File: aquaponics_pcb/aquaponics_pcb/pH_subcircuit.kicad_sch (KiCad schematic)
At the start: 4 parts, among them J1 RFPC-SMA27-F, U1 Atlas Scientific EZO

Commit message: finish MCU and start logic isolation block
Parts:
- J1: footprint RFPCSMA27F -> SamacSys_Parts:RFPCSMA27F
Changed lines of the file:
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@@
 			)
 		)
-		(property "Footprint" "RFPCSMA27F"
+		(property "Footprint" "SamacSys_Parts:RFPCSMA27F"
 			(at 179.07 187.63 0)
 			(effects

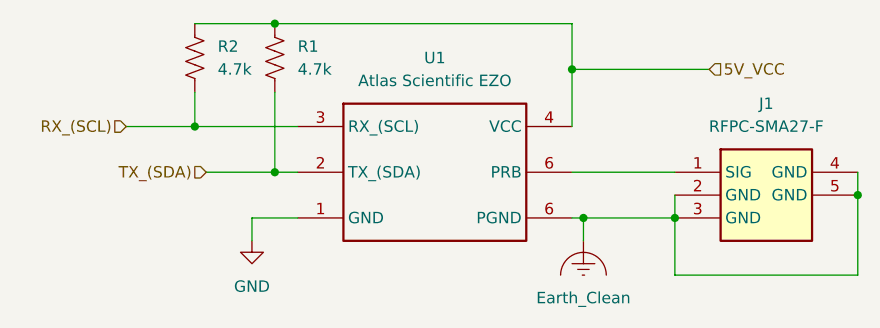
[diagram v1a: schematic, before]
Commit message: begin motor control sch
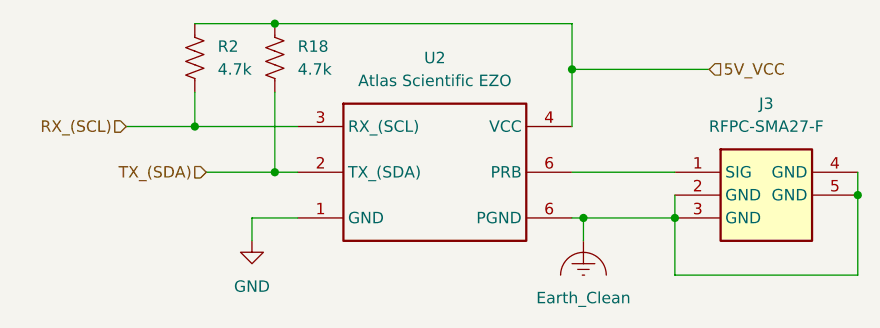
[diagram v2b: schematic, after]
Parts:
- renumbered J1 to J3, R1 to R18, U1 to U2
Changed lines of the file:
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@@
 		(instances
 			(project "aquaponics_pcb"
+				(path "/c5e5a8d2-0dcc-4520-98a5-511e1dc0d12f/07c81ada-4777-4a98-b82e-c983cee6a37c"
+					(reference "R17")
+					(unit 1)
+				)
 				(path "/c5e5a8d2-0dcc-4520-98a5-511e1dc0d12f/37a12f26-e0b7-4740-be24-dc513a8a30de"
 					(reference "R2")
+					(unit 1)
+				)
+				(path "/c5e5a8d2-0dcc-4520-98a5-511e1dc0d12f/a6edc2ac-dd2e-4ead-b353-200a5e98d0aa"
+					(reference "R1")
 					(unit 1)
 				)
@@
 		(dnp no)
 		(fields_autoplaced yes)
-		(property "Reference" "#PWR02"
+		(property "Reference" "#PWR027"
 			(at 152.4 107.95 0)
 			(effects
@@
 		)
 		(instances
-			(project ""
-				(path "/c5e5a8d2-0dcc-4520-98a5-511e1dc0d12f/37a12f26-e0b7-4740-be24-dc513a8a30de"
+			(project "aquaponics_pcb"
+				(path "/c5e5a8d2-0dcc-4520-98a5-511e1dc0d12f/07c81ada-4777-4a98-b82e-c983cee6a37c"
+					(reference "#PWR027")
+					(unit 1)
+				)
+				(path "/c5e5a8d2-0dcc-4520-98a5-511e1dc0d12f/37a12f26-e0b7-4740-be24-dc513a8a30de"
+					(reference "#PWR027")
+					(unit 1)
+				)
+				(path "/c5e5a8d2-0dcc-4520-98a5-511e1dc0d12f/a6edc2ac-dd2e-4ead-b353-200a5e98d0aa"
 					(reference "#PWR02")
 					(unit 1)
@@
 		(dnp no)
 		(fields_autoplaced yes)
-		(property "Reference" "U1"
+		(property "Reference" "U2"
 			(at 135.89 80.01 0)
 			(effects
@@
 		)
 		(instances
-			(project ""
-				(path "/c5e5a8d2-0dcc-4520-98a5-511e1dc0d12f/37a12f26-e0b7-4740-be24-dc513a8a30de"
+			(project "aquaponics_pcb"
+				(path "/c5e5a8d2-0dcc-4520-98a5-511e1dc0d12f/07c81ada-4777-4a98-b82e-c983cee6a37c"
+					(reference "U2")
+					(unit 1)
+				)
+				(path "/c5e5a8d2-0dcc-4520-98a5-511e1dc0d12f/37a12f26-e0b7-4740-be24-dc513a8a30de"
+					(reference "U2")
+					(unit 1)
+				)
+				(path "/c5e5a8d2-0dcc-4520-98a5-511e1dc0d12f/a6edc2ac-dd2e-4ead-b353-200a5e98d0aa"
 					(reference "U1")
 					(unit 1)
@@
 		(dnp no)
 		(fields_autoplaced yes)
-		(property "Reference" "R1"
+		(property "Reference" "R18"
 			(at 120.65 78.7399 0)
 			(effects
@@
 		)
 		(instances
-			(project ""
-				(path "/c5e5a8d2-0dcc-4520-98a5-511e1dc0d12f/37a12f26-e0b7-4740-be24-dc513a8a30de"
-					(reference "R1")
+			(project "aquaponics_pcb"
+				(path "/c5e5a8d2-0dcc-4520-98a5-511e1dc0d12f/07c81ada-4777-4a98-b82e-c983cee6a37c"
+					(reference "R18")
+					(unit 1)
+				)
+				(path "/c5e5a8d2-0dcc-4520-98a5-511e1dc0d12f/37a12f26-e0b7-4740-be24-dc513a8a30de"
+					(reference "R18")
+					(unit 1)
+				)
+				(path "/c5e5a8d2-0dcc-4520-98a5-511e1dc0d12f/a6edc2ac-dd2e-4ead-b353-200a5e98d0aa"
+					(reference "R19")
 					(unit 1)
 				)
@@
 		(dnp no)
 		(fields_autoplaced yes)
-		(property "Reference" "J1"
+		(property "Reference" "J3"
 			(at 172.72 85.09 0)
 			(effects
@@
 		)
 		(instances
-			(project ""
-				(path "/c5e5a8d2-0dcc-4520-98a5-511e1dc0d12f/37a12f26-e0b7-4740-be24-dc513a8a30de"
+			(project "aquaponics_pcb"
+				(path "/c5e5a8d2-0dcc-4520-98a5-511e1dc0d12f/07c81ada-4777-4a98-b82e-c983cee6a37c"
+					(reference "J3")
+					(unit 1)
+				)
+				(path "/c5e5a8d2-0dcc-4520-98a5-511e1dc0d12f/37a12f26-e0b7-4740-be24-dc513a8a30de"
+					(reference "J3")
+					(unit 1)
+				)
+				(path "/c5e5a8d2-0dcc-4520-98a5-511e1dc0d12f/a6edc2ac-dd2e-4ead-b353-200a5e98d0aa"
 					(reference "J1")
 					(unit 1)
@@
 		(dnp no)
 		(fields_autoplaced yes)
-		(property "Reference" "#PWR01"
+		(property "Reference" "#PWR026"
 			(at 115.57 106.68 0)
 			(effects
@@
 		)
 		(instances
-			(project ""
-				(path "/c5e5a8d2-0dcc-4520-98a5-511e1dc0d12f/37a12f26-e0b7-4740-be24-dc513a8a30de"
+			(project "aquaponics_pcb"
+				(path "/c5e5a8d2-0dcc-4520-98a5-511e1dc0d12f/07c81ada-4777-4a98-b82e-c983cee6a37c"
+					(reference "#PWR026")
+					(unit 1)
+				)
+				(path "/c5e5a8d2-0dcc-4520-98a5-511e1dc0d12f/37a12f26-e0b7-4740-be24-dc513a8a30de"
+					(reference "#PWR026")
+					(unit 1)
+				)
+				(path "/c5e5a8d2-0dcc-4520-98a5-511e1dc0d12f/a6edc2ac-dd2e-4ead-b353-200a5e98d0aa"
 					(reference "#PWR01")
 					(unit 1)

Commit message: add ezo datasheets, update motor schematic and add 2 motors
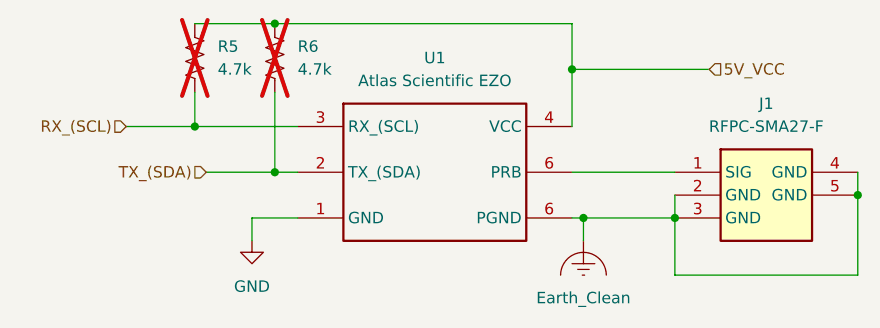
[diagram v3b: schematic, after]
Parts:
- R5: renamed from R2; now not fitted
- R6: renamed from R18; now not fitted
- renumbered J3 to J1, U2 to U1
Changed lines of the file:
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@@
 		(in_bom yes)
 		(on_board yes)
-		(dnp no)
+		(dnp yes)
 		(fields_autoplaced yes)
-		(property "Reference" "R2"
+		(property "Reference" "R5"
 			(at 111.76 78.7399 0)
 			(effects
@@
 			(project "aquaponics_pcb"
 				(path "/c5e5a8d2-0dcc-4520-98a5-511e1dc0d12f/07c81ada-4777-4a98-b82e-c983cee6a37c"
-					(reference "R17")
+					(reference "R19")
 					(unit 1)
 				)
 				(path "/c5e5a8d2-0dcc-4520-98a5-511e1dc0d12f/37a12f26-e0b7-4740-be24-dc513a8a30de"
-					(reference "R2")
+					(reference "R5")
 					(unit 1)
 				)
 				(path "/c5e5a8d2-0dcc-4520-98a5-511e1dc0d12f/a6edc2ac-dd2e-4ead-b353-200a5e98d0aa"
-					(reference "R1")
+					(reference "R21")
 					(unit 1)
 				)
@@
 		(dnp no)
 		(fields_autoplaced yes)
-		(property "Reference" "#PWR027"
+		(property "Reference" "#PWR02"
 			(at 152.4 107.95 0)
 			(effects
@@
 			(project "aquaponics_pcb"
 				(path "/c5e5a8d2-0dcc-4520-98a5-511e1dc0d12f/07c81ada-4777-4a98-b82e-c983cee6a37c"
-					(reference "#PWR027")
+					(reference "#PWR030")
 					(unit 1)
 				)
 				(path "/c5e5a8d2-0dcc-4520-98a5-511e1dc0d12f/37a12f26-e0b7-4740-be24-dc513a8a30de"
-					(reference "#PWR027")
+					(reference "#PWR02")
 					(unit 1)
 				)
 				(path "/c5e5a8d2-0dcc-4520-98a5-511e1dc0d12f/a6edc2ac-dd2e-4ead-b353-200a5e98d0aa"
-					(reference "#PWR02")
+					(reference "#PWR032")
 					(unit 1)
 				)
@@
 		(dnp no)
 		(fields_autoplaced yes)
-		(property "Reference" "U2"
+		(property "Reference" "U1"
 			(at 135.89 80.01 0)
 			(effects
@@
 				)
 				(path "/c5e5a8d2-0dcc-4520-98a5-511e1dc0d12f/37a12f26-e0b7-4740-be24-dc513a8a30de"
-					(reference "U2")
+					(reference "U1")
 					(unit 1)
 				)
 				(path "/c5e5a8d2-0dcc-4520-98a5-511e1dc0d12f/a6edc2ac-dd2e-4ead-b353-200a5e98d0aa"
-					(reference "U1")
+					(reference "U3")
 					(unit 1)
 				)
@@
 		(in_bom yes)
 		(on_board yes)
-		(dnp no)
+		(dnp yes)
 		(fields_autoplaced yes)
-		(property "Reference" "R18"
+		(property "Reference" "R6"
 			(at 120.65 78.7399 0)
 			(effects
@@
 			(project "aquaponics_pcb"
 				(path "/c5e5a8d2-0dcc-4520-98a5-511e1dc0d12f/07c81ada-4777-4a98-b82e-c983cee6a37c"
-					(reference "R18")
+					(reference "R20")
 					(unit 1)
 				)
 				(path "/c5e5a8d2-0dcc-4520-98a5-511e1dc0d12f/37a12f26-e0b7-4740-be24-dc513a8a30de"
-					(reference "R18")
+					(reference "R6")
 					(unit 1)
 				)
 				(path "/c5e5a8d2-0dcc-4520-98a5-511e1dc0d12f/a6edc2ac-dd2e-4ead-b353-200a5e98d0aa"
-					(reference "R19")
+					(reference "R22")
 					(unit 1)
 				)
@@
 		(dnp no)
 		(fields_autoplaced yes)
-		(property "Reference" "J3"
+		(property "Reference" "J1"
 			(at 172.72 85.09 0)
 			(effects
@@
 				)
 				(path "/c5e5a8d2-0dcc-4520-98a5-511e1dc0d12f/37a12f26-e0b7-4740-be24-dc513a8a30de"
-					(reference "J3")
+					(reference "J1")
 					(unit 1)
 				)
 				(path "/c5e5a8d2-0dcc-4520-98a5-511e1dc0d12f/a6edc2ac-dd2e-4ead-b353-200a5e98d0aa"
-					(reference "J1")
+					(reference "J4")
 					(unit 1)
 				)
@@
 		(dnp no)
 		(fields_autoplaced yes)
-		(property "Reference" "#PWR026"
+		(property "Reference" "#PWR01"
 			(at 115.57 106.68 0)
 			(effects
@@
 			(project "aquaponics_pcb"
 				(path "/c5e5a8d2-0dcc-4520-98a5-511e1dc0d12f/07c81ada-4777-4a98-b82e-c983cee6a37c"
-					(reference "#PWR026")
+					(reference "#PWR029")
 					(unit 1)
 				)
 				(path "/c5e5a8d2-0dcc-4520-98a5-511e1dc0d12f/37a12f26-e0b7-4740-be24-dc513a8a30de"
-					(reference "#PWR026")
+					(reference "#PWR01")
 					(unit 1)
 				)
 				(path "/c5e5a8d2-0dcc-4520-98a5-511e1dc0d12f/a6edc2ac-dd2e-4ead-b353-200a5e98d0aa"
-					(reference "#PWR01")
-					(unit 1)
-				)
+					(reference "#PWR031")
+					(unit 1)
+				)

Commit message: add initial pcb layout
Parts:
- U1: footprint (none) -> aquaponics_pcb:EZO FOOTPRINT
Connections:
- net at J1.1 (SIG): now also U1.5 (PRB); no longer U1.6 (PRB)
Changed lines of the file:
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@@
 			)
 		)
-		(property "Footprint" ""
+		(property "Footprint" "aquaponics_pcb:EZO FOOTPRINT"
 			(at 125.73 100.33 0)
 			(effects
@@
 		(pin "4"
 		)
-		(pin "6"
+		(pin "5"
 		)
 		(instances

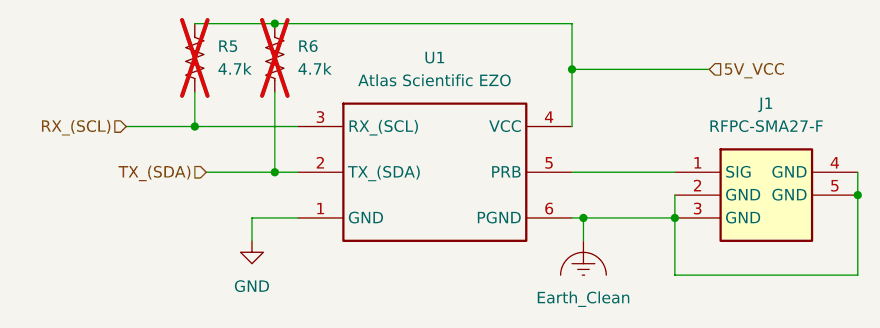
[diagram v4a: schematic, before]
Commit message: Update PCB: add ADM3260, replace C3 with SMA connector
Replaced C3 capacitor footprint with an RFPC-SMA27-F SMA connector and added the ADM3260ARSZ digital isolator (IC3) to the PCB. Updated R3 to a 10k resistor and made related netlist and footprint changes.
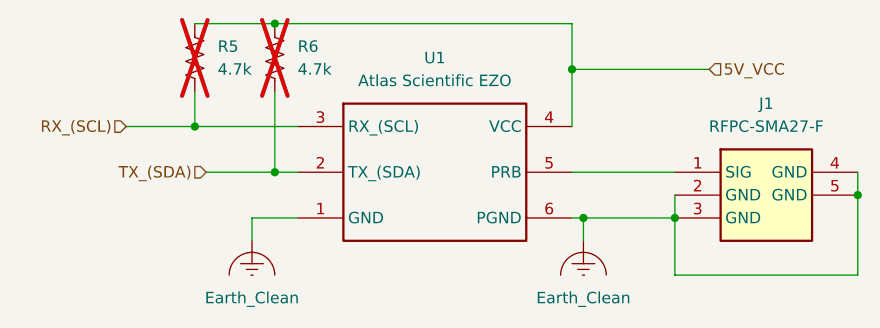
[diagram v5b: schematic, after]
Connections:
- net GND is gone; now on net Earth_Clean: U1.1 (GND)
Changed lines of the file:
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@@
+	(symbol
+		(lib_id "power:Earth_Clean")
+		(at 115.57 100.33 0)
+		(unit 1)
+		(exclude_from_sim no)
+		(in_bom yes)
+		(on_board yes)
+		(dnp no)
+		(fields_autoplaced yes)
+		(property "Reference" "#PWR01"
+			(at 115.57 107.95 0)
+			(effects
+				(font
+					(size 1.27 1.27)
+				)
+				(hide yes)
+			)
+		)
+		(property "Value" "Earth_Clean"
+			(at 115.57 106.68 0)
+			(effects
+				(font
+					(size 1.27 1.27)
+				)
+			)
+		)
+		(property "Footprint" ""
+			(at 115.57 101.6 0)
+			(effects
+				(font
+					(size 1.27 1.27)
+				)
+				(hide yes)
+			)
+		)
+		(property "Datasheet" "~"
+			(at 115.57 101.6 0)
+			(effects
+				(font
+					(size 1.27 1.27)
+				)
+				(hide yes)
+			)
+		)
+		(property "Description" "Power symbol creates a global label with name \"Earth_Clean\""
+			(at 115.57 100.33 0)
+			(effects
+				(font
+					(size 1.27 1.27)
+				)
+				(hide yes)
+			)
+		)
+		(pin "1"
+		)
+		(instances
+			(project "aquaponics_pcb"
+				(path "/c5e5a8d2-0dcc-4520-98a5-511e1dc0d12f/07c81ada-4777-4a98-b82e-c983cee6a37c"
+					(reference "#PWR029")
+					(unit 1)
+				)
+				(path "/c5e5a8d2-0dcc-4520-98a5-511e1dc0d12f/37a12f26-e0b7-4740-be24-dc513a8a30de"
+					(reference "#PWR01")
+					(unit 1)
+				)
+				(path "/c5e5a8d2-0dcc-4520-98a5-511e1dc0d12f/a6edc2ac-dd2e-4ead-b353-200a5e98d0aa"
+					(reference "#PWR031")
+					(unit 1)
+				)
+			)
+		)
+	)
 	(symbol
 		(lib_id "power:Earth_Clean")
@@
 					(unit 1)
 				)
-			)
-		)
-	)
-	(symbol
-		(lib_id "power:GND")
-		(at 115.57 100.33 0)
-		(unit 1)
-		(exclude_from_sim no)
-		(in_bom yes)
-		(on_board yes)
-		(dnp no)
-		(fields_autoplaced yes)
-		(property "Reference" "#PWR01"
-			(at 115.57 106.68 0)
-			(effects
-				(font
-					(size 1.27 1.27)
-				)
-				(hide yes)
-			)
-		)
-		(property "Value" "GND"
-			(at 115.57 105.41 0)
-			(effects
-				(font
-					(size 1.27 1.27)
-				)
-			)
-		)
-		(property "Footprint" ""
-			(at 115.57 100.33 0)
-			(effects
-				(font
-					(size 1.27 1.27)
-				)
-				(hide yes)
-			)
-		)
-		(property "Datasheet" ""
-			(at 115.57 100.33 0)
-			(effects
-				(font
-					(size 1.27 1.27)
-				)
-				(hide yes)
-			)
-		)
-		(property "Description" "Power symbol creates a global label with name \"GND\" , ground"
-			(at 115.57 100.33 0)
-			(effects
-				(font
-					(size 1.27 1.27)
-				)
-				(hide yes)
-			)
-		)
-		(pin "1"
-		)
-		(instances
-			(project "aquaponics_pcb"
-				(path "/c5e5a8d2-0dcc-4520-98a5-511e1dc0d12f/07c81ada-4777-4a98-b82e-c983cee6a37c"
-					(reference "#PWR029")
-					(unit 1)
-				)
-				(path "/c5e5a8d2-0dcc-4520-98a5-511e1dc0d12f/37a12f26-e0b7-4740-be24-dc513a8a30de"
-					(reference "#PWR01")
-					(unit 1)
-				)
-				(path "/c5e5a8d2-0dcc-4520-98a5-511e1dc0d12f/a6edc2ac-dd2e-4ead-b353-200a5e98d0aa"
-					(reference "#PWR031")
-					(unit 1)
-				)

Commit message: finish ground and power pours. fix rules and run final DRC. export gerbers
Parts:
- R5, R6: LCSC Part Number (none) -> C99782
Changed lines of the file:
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@@
+			)
+		)
+		(property "LCSC Part Number" "C99782"
+			(at 109.22 80.01 0)
+			(effects
+				(font
+					(size 1.27 1.27)
+				)
+				(hide yes)
+			)
+		)
+		(property "JLCPCB Part #" ""
+			(at 109.22 80.01 0)
+			(effects
+				(font
+					(size 1.27 1.27)
+				)
+				(hide yes)
 			)
 		)
@@
 			)
 		)
+		(property "LCSC Part Number" ""
+			(at 125.73 100.33 0)
+			(effects
+				(font
+					(size 1.27 1.27)
+				)
+				(hide yes)
+			)
+		)
+		(property "JLCPCB Part #" ""
+			(at 125.73 100.33 0)
+			(effects
+				(font
+					(size 1.27 1.27)
+				)
+				(hide yes)
+			)
+		)
 		(pin "3"
 		)
@@
 			)
 		)
+		(property "LCSC Part Number" "C99782"
+			(at 118.11 80.01 0)
+			(effects
+				(font
+					(size 1.27 1.27)
+				)
+				(hide yes)
+			)
+		)
+		(property "JLCPCB Part #" ""
+			(at 118.11 80.01 0)
+			(effects
+				(font
+					(size 1.27 1.27)
+				)
+				(hide yes)
+			)
+		)
 		(pin "1"
 		)
@@
 				(hide yes)
 			)
+		)
+		(property "LCSC Part Number" ""
+			(at 162.56 92.71 0)
+			(effects
+				(font
+					(size 1.27 1.27)
+				)
+				(hide yes)
+			)
+		)
+		(property "JLCPCB Part #" ""
+			(at 162.56 92.71 0)
+			(effects
+				(font
+					(size 1.27 1.27)
+				)
+				(hide yes)
+			)
